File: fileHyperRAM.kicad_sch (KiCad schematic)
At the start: 15 parts, among them U4 W957A8MFYA

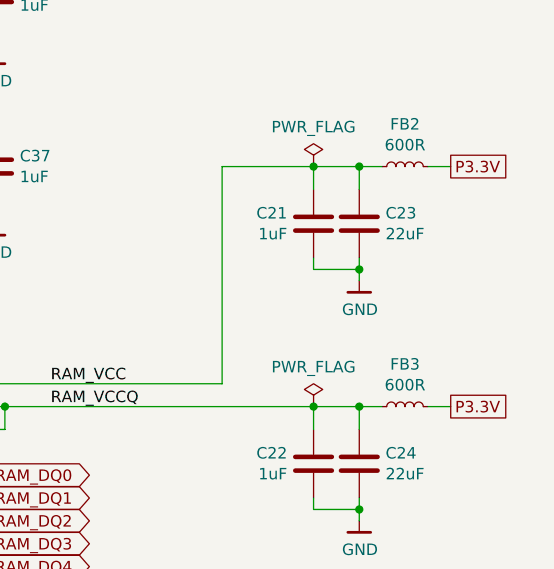
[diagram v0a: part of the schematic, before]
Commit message: Convert to KiCAD 7
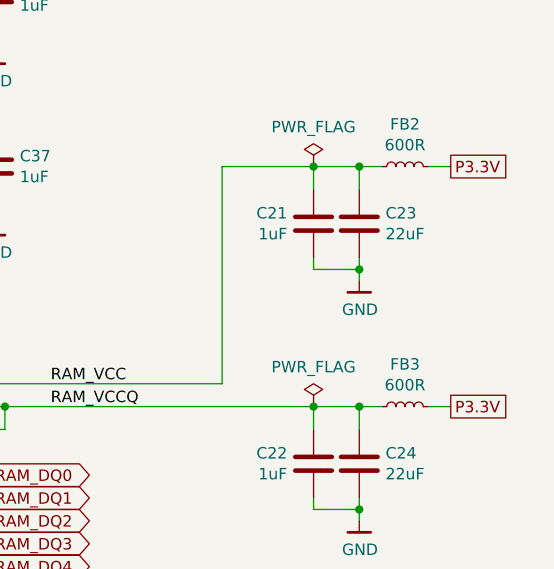
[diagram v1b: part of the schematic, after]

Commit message: Update component prices
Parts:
- C21, C22, C34, C35, C36, C37: Pricing (EUR) 0,10 -> 0,09
- C23, C24: Pricing (EUR) 0,22 -> 0,19
- FB2, FB3: Pricing (EUR) 0,12 -> 0,09
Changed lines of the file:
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@@
       (effects (font (size 1.27 1.27)) hide)
     )
-    (property "Pricing (EUR)" "0,10" (at 82.55 50.8 0)
+    (property "Pricing (EUR)" "0,09" (at 82.55 50.8 0)
       (effects (font (size 1.27 1.27)) hide)
     )
@@
       (effects (font (size 1.27 1.27)) hide)
     )
-    (property "Pricing (EUR)" "0,10" (at 87.63 50.8 0)
+    (property "Pricing (EUR)" "0,09" (at 87.63 50.8 0)
       (effects (font (size 1.27 1.27)) hide)
     )
@@
       (effects (font (size 1.27 1.27)) hide)
     )
-    (property "Pricing (EUR)" "0,10" (at 82.55 31.75 0)
+    (property "Pricing (EUR)" "0,09" (at 82.55 31.75 0)
       (effects (font (size 1.27 1.27)) hide)
     )
@@
       (effects (font (size 1.27 1.27)) hide)
     )
-    (property "Pricing (EUR)" "0,10" (at 87.63 31.75 0)
+    (property "Pricing (EUR)" "0,09" (at 87.63 31.75 0)
       (effects (font (size 1.27 1.27)) hide)
     )
@@
       (effects (font (size 1.27 1.27)) hide)
     )
-    (property "Pricing (EUR)" "0,10" (at 123.19 57.15 0)
+    (property "Pricing (EUR)" "0,09" (at 123.19 57.15 0)
       (effects (font (size 1.27 1.27)) hide)
     )
@@
       (effects (font (size 1.27 1.27)) hide)
     )
-    (property "Pricing (EUR)" "0,22" (at 128.27 57.15 0)
+    (property "Pricing (EUR)" "0,19" (at 128.27 57.15 0)
       (effects (font (size 1.27 1.27)) hide)
     )
@@
       (effects (font (size 1.27 1.27)) hide)
     )
-    (property "Pricing (EUR)" "0,12" (at 133.35 50.8 0)
+    (property "Pricing (EUR)" "0,09" (at 133.35 50.8 0)
       (effects (font (size 1.27 1.27)) hide)
     )
@@
       (effects (font (size 1.27 1.27)) hide)
     )
-    (property "Pricing (EUR)" "0,10" (at 123.19 83.82 0)
+    (property "Pricing (EUR)" "0,09" (at 123.19 83.82 0)
       (effects (font (size 1.27 1.27)) hide)
     )
@@
       (effects (font (size 1.27 1.27)) hide)
     )
-    (property "Pricing (EUR)" "0,22" (at 128.27 83.82 0)
+    (property "Pricing (EUR)" "0,19" (at 128.27 83.82 0)
       (effects (font (size 1.27 1.27)) hide)
     )
@@
       (effects (font (size 1.27 1.27)) hide)
     )
-    (property "Pricing (EUR)" "0,12" (at 133.35 77.47 0)
-      (effects (font (size 1.27 1.27)) hide)
-    )
+    (property "Pricing (EUR)" "0,09" (at 133.35 77.47 0)
+      (effects (font (size 1.27 1.27)) hide)
+    )
